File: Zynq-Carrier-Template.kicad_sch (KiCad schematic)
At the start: 5 parts, among them J1 Zynq_SoM

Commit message: Testing collab functionality
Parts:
- added J3: USB_C_Receptacle_USB2.0_16P, Connector_USB:USB_C_Receptacle_G-Switch_GT-USB-7010ASV, symbol Connector:USB_C_Receptacle_USB2.0_16P
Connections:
- new net: J3.A1 (GND), J3.A12 (GND), J3.B1 (GND), J3.B12 (GND)
- new net: J3.A4 (VBUS), J3.A9 (VBUS), J3.B4 (VBUS), J3.B9 (VBUS)
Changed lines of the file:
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@@
+	)
+	(symbol
+		(lib_id "Connector:USB_C_Receptacle_USB2.0_16P")
+		(at 232.41 130.81 0)
+		(unit 1)
+		(exclude_from_sim no)
+		(in_bom yes)
+		(on_board yes)
+		(dnp no)
+		(fields_autoplaced yes)
+		(property "Reference" "J3"
+			(at 232.41 107.95 0)
+			(effects
+				(font
+					(size 1.27 1.27)
+				)
+			)
+		)
+		(property "Value" "USB_C_Receptacle_USB2.0_16P"
+			(at 232.41 110.49 0)
+			(effects
+				(font
+					(size 1.27 1.27)
+				)
+			)
+		)
+		(property "Footprint" "Connector_USB:USB_C_Receptacle_G-Switch_GT-USB-7010ASV"
+			(at 236.22 130.81 0)
+			(effects
+				(font
+					(size 1.27 1.27)
+				)
+				(hide yes)
+			)
+		)
+		(property "Datasheet" "https://www.usb.org/sites/default/files/documents/usb_type-c.zip"
+			(at 236.22 130.81 0)
+			(effects
+				(font
+					(size 1.27 1.27)
+				)
+				(hide yes)
+			)
+		)
+		(property "Description" "USB 2.0-only 16P Type-C Receptacle connector"
+			(at 232.41 130.81 0)
+			(effects
+				(font
+					(size 1.27 1.27)
+				)
+				(hide yes)
+			)
+		)
+		(pin "A9"
+		)
+		(pin "A6"
+		)
+		(pin "A12"
+		)
+		(pin "B7"
+		)
+		(pin "B9"
+		)
+		(pin "B8"
+		)
+		(pin "B6"
+		)
+		(pin "A5"
+		)
+		(pin "B5"
+		)
+		(pin "B1"
+		)
+		(pin "A7"
+		)
+		(pin "A1"
+		)
+		(pin "A8"
+		)
+		(pin "A4"
+		)
+		(pin "B12"
+		)
+		(pin "S1"
+		)
+		(pin "B4"
+		)
+		(instances
+			(project ""
+				(path "/e0c786d3-4c71-488f-94d1-904eb052c2b4"
+					(reference "J3")
+					(unit 1)
+				)
+			)
+		)
 	)
 	(symbol

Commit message: Import BQ25629RYKR
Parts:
- added U1: BQ25629RYKR, BQ25629RYKR:RYK0018A-MFG, symbol BQ25629RYKR:BQ25629RYKR
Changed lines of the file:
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@@
+	)
+	(symbol
+		(lib_id "BQ25629RYKR:BQ25629RYKR")
+		(at 217.17 49.53 0)
+		(unit 1)
+		(exclude_from_sim no)
+		(in_bom yes)
+		(on_board yes)
+		(dnp no)
+		(fields_autoplaced yes)
+		(property "Reference" "U1"
+			(at 236.22 39.37 0)
+			(effects
+				(font
+					(size 1.524 1.524)
+				)
+			)
+		)
+		(property "Value" "BQ25629RYKR"
+			(at 236.22 41.91 0)
+			(effects
+				(font
+					(size 1.524 1.524)
+				)
+			)
+		)
+		(property "Footprint" "BQ25629RYKR:RYK0018A-MFG"
+			(at 217.17 49.53 0)
+			(effects
+				(font
+					(size 1.27 1.27)
+					(italic yes)
+				)
+				(hide yes)
+			)
+		)
+		(property "Datasheet" "https://www.ti.com/lit/gpn/bq25629"
+			(at 217.17 49.53 0)
+			(effects
+				(font
+					(size 1.27 1.27)
+					(italic yes)
+				)
+				(hide yes)
+			)
+		)
+		(property "Description" ""
+			(at 217.17 49.53 0)
+			(effects
+				(font
+					(size 1.27 1.27)
+				)
+				(hide yes)
+			)
+		)
+		(pin "17"
+		)
+		(pin "10"
+		)
+		(pin "18"
+		)
+		(pin "14"
+		)
+		(pin "3"
+		)
+		(pin "15"
+		)
+		(pin "7"
+		)
+		(pin "5"
+		)
+		(pin "8"
+		)
+		(pin "16"
+		)
+		(pin "1"
+		)
+		(pin "6"
+		)
+		(pin "9"
+		)
+		(pin "2"
+		)
+		(pin "4"
+		)
+		(pin "13"
+		)
+		(pin "11"
+		)
+		(pin "12"
+		)
+		(instances
+			(project ""
+				(path "/e0c786d3-4c71-488f-94d1-904eb052c2b4"
+					(reference "U1")
+					(unit 1)
+				)
+			)
+		)
 	)
 	(symbol

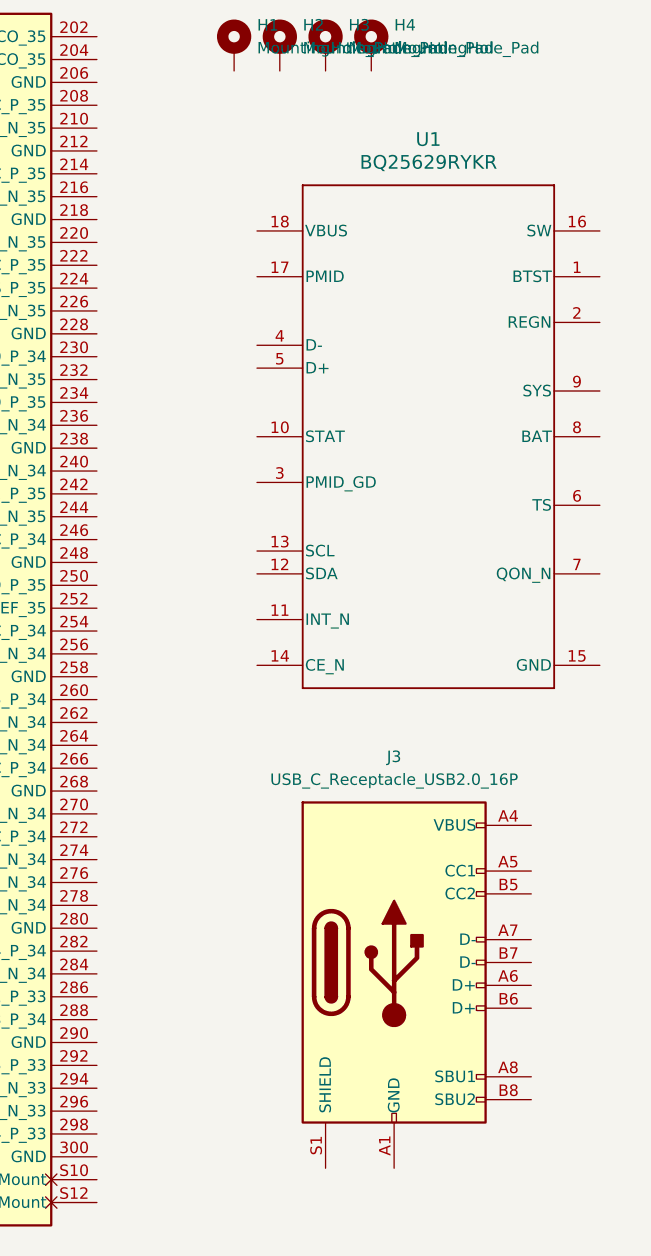
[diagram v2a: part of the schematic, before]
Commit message: Copper Fill demo
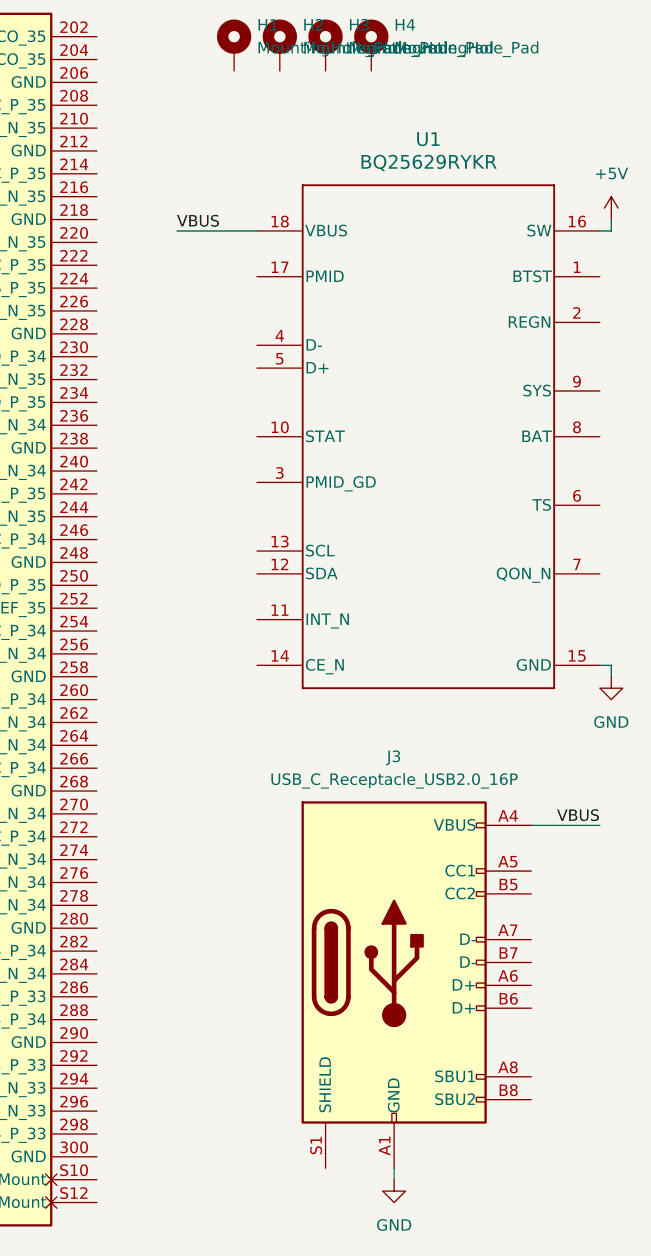
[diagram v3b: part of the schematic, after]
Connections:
- net GND: now reaches J3.A1 (GND), J3.A12 (GND), J3.B1 (GND), J3.B12 (GND)
- net GND: now also U1.15 (GND)
- net VBUS: now reaches J3.A4 (VBUS), J3.A9 (VBUS), J3.B4 (VBUS), J3.B9 (VBUS)
- net VBUS: now also U1.18 (VBUS)
- net +5V: now reaches U1.16 (SW)

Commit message: Import 1uH Inductor
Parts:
- added L1: P3519R-102J, 1uH_Inductor:IND_P3519R_API, symbol 1uH_Inductor:P3519R-102J
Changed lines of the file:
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@@
 (kicad_sch
-	(version 20231120)
+	(version 20250114)
 	(generator "eeschema")
-	(generator_version "8.0")
+	(generator_version "9.0")
 	(paper "A4")
 	(wire
@@
 	(label "VBUS"
 		(at 208.28 49.53 0)
-		(fields_autoplaced yes)
 		(effects
 			(font
@@
 	(label "VBUS"
 		(at 255.27 115.57 180)
-		(fields_autoplaced yes)
 		(effects
 			(font
@@
 	)
 	(symbol
+		(lib_id "1uH_Inductor:P3519R-102J")
+		(at 261.62 33.02 0)
+		(unit 1)
+		(exclude_from_sim no)
+		(in_bom yes)
+		(on_board yes)
+		(dnp no)
+		(fields_autoplaced yes)
+		(property "Reference" "L1"
+			(at 269.24 25.4 0)
+			(effects
+				(font
+					(size 1.524 1.524)
+				)
+			)
+		)
+		(property "Value" "P3519R-102J"
+			(at 269.24 27.94 0)
+			(effects
+				(font
+					(size 1.524 1.524)
+				)
+			)
+		)
+		(property "Footprint" "1uH_Inductor:IND_P3519R_API"
+			(at 261.62 33.02 0)
+			(effects
+				(font
+					(size 1.27 1.27)
+					(italic yes)
+				)
+				(hide yes)
+			)
+		)
+		(property "Datasheet" "P3519R-102J"
+			(at 261.62 33.02 0)
+			(effects
+				(font
+					(size 1.27 1.27)
+					(italic yes)
+				)
+				(hide yes)
+			)
+		)
+		(property "Description" ""
+			(at 261.62 33.02 0)
+			(effects
+				(font
+					(size 1.27 1.27)
+				)
+				(hide yes)
+			)
+		)
+		(pin "1"
+		)
+		(pin "2"
+		)
+		(instances
+			(project ""
+				(path "/e0c786d3-4c71-488f-94d1-904eb052c2b4"
+					(reference "L1")
+					(unit 1)
+				)
+			)
+		)
+	)
+	(symbol
 		(lib_id "Mechanical:MountingHole_Pad")
 		(at 219.71 29.21 0)
@@
 		)
 	)
+	(embedded_fonts no)
 )

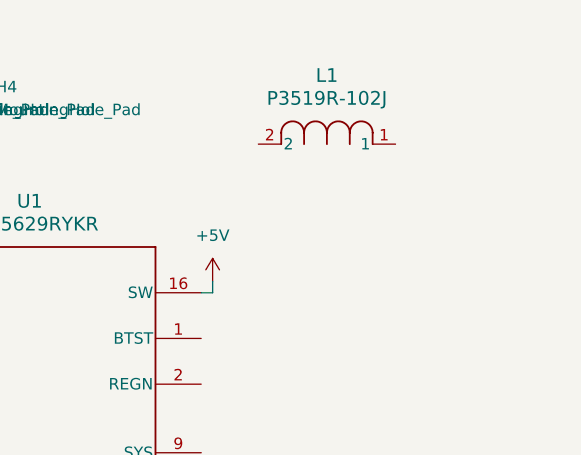
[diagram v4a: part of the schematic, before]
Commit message: Import JST_Pins and Inductor
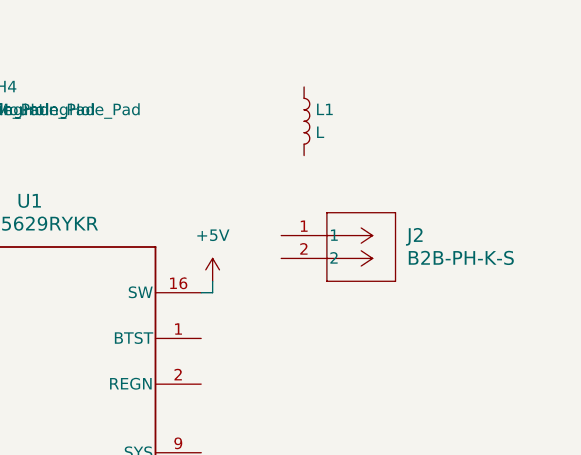
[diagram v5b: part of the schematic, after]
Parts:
- removed L1: P3519R-102J, 1uH_Inductor:IND_P3519R_API, symbol 1uH_Inductor:P3519R-102J
- added J2: B2B-PH-K-S, CONN2_B2B-PH-K-S_JST, symbol JST_Pins:B2B-PH-K-S
- added L1: L, Inductor_SMD:L_1008_2520Metric_Pad1.43x2.20mm_HandSolder, symbol Device:L
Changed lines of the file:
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@@
+	)
+	(symbol
+		(lib_id "JST_Pins:B2B-PH-K-S")
+		(at 264.16 43.18 0)
+		(unit 1)
+		(exclude_from_sim no)
+		(in_bom yes)
+		(on_board yes)
+		(dnp no)
+		(fields_autoplaced yes)
+		(property "Reference" "J2"
+			(at 278.13 43.1799 0)
+			(effects
+				(font
+					(size 1.524 1.524)
+				)
+				(justify left)
+			)
+		)
+		(property "Value" "B2B-PH-K-S"
+			(at 278.13 45.7199 0)
+			(effects
+				(font
+					(size 1.524 1.524)
+				)
+				(justify left)
+			)
+		)
+		(property "Footprint" "CONN2_B2B-PH-K-S_JST"
+			(at 264.16 43.18 0)
+			(effects
+				(font
+					(size 1.27 1.27)
+					(italic yes)
+				)
+				(hide yes)
+			)
+		)
+		(property "Datasheet" "B2B-PH-K-S"
+			(at 264.16 43.18 0)
+			(effects
+				(font
+					(size 1.27 1.27)
+					(italic yes)
+				)
+				(hide yes)
+			)
+		)
+		(property "Description" ""
+			(at 264.16 43.18 0)
+			(effects
+				(font
+					(size 1.27 1.27)
+				)
+				(hide yes)
+			)
+		)
+		(pin "2"
+		)
+		(pin "1"
+		)
+		(instances
+			(project ""
+				(path "/e0c786d3-4c71-488f-94d1-904eb052c2b4"
+					(reference "J2")
+					(unit 1)
+				)
+			)
+		)
 	)
 	(symbol
@@
 	)
 	(symbol
+		(lib_id "Device:L")
+		(at 266.7 30.48 0)
+		(unit 1)
+		(exclude_from_sim no)
+		(in_bom yes)
+		(on_board yes)
+		(dnp no)
+		(fields_autoplaced yes)
+		(property "Reference" "L1"
+			(at 267.97 29.2099 0)
+			(effects
+				(font
+					(size 1.27 1.27)
+				)
+				(justify left)
+			)
+		)
+		(property "Value" "L"
+			(at 267.97 31.7499 0)
+			(effects
+				(font
+					(size 1.27 1.27)
+				)
+				(justify left)
+			)
+		)
+		(property "Footprint" "Inductor_SMD:L_1008_2520Metric_Pad1.43x2.20mm_HandSolder"
+			(at 266.7 30.48 0)
+			(effects
+				(font
+					(size 1.27 1.27)
+				)
+				(hide yes)
+			)
+		)
+		(property "Datasheet" "~"
+			(at 266.7 30.48 0)
+			(effects
+				(font
+					(size 1.27 1.27)
+				)
+				(hide yes)
+			)
+		)
+		(property "Description" "Inductor"
+			(at 266.7 30.48 0)
+			(effects
+				(font
+					(size 1.27 1.27)
+				)
+				(hide yes)
+			)
+		)
+		(pin "2"
+		)
+		(pin "1"
+		)
+		(instances
+			(project ""
+				(path "/e0c786d3-4c71-488f-94d1-904eb052c2b4"
+					(reference "L1")
+					(unit 1)
+				)
+			)
+		)
+	)
+	(symbol
 		(lib_id "symbol_Zynq_SoM:Zynq_SoM")
 		(at 22.86 27.94 0)
@@
 					(unit 1)
 				)
-			)
-		)
-	)
-	(symbol
-		(lib_id "1uH_Inductor:P3519R-102J")
-		(at 261.62 33.02 0)
-		(unit 1)
-		(exclude_from_sim no)
-		(in_bom yes)
-		(on_board yes)
-		(dnp no)
-		(fields_autoplaced yes)
-		(property "Reference" "L1"
-			(at 269.24 25.4 0)
-			(effects
-				(font
-					(size 1.524 1.524)
-				)
-			)
-		)
-		(property "Value" "P3519R-102J"
-			(at 269.24 27.94 0)
-			(effects
-				(font
-					(size 1.524 1.524)
-				)
-			)
-		)
-		(property "Footprint" "1uH_Inductor:IND_P3519R_API"
-			(at 261.62 33.02 0)
-			(effects
-				(font
-					(size 1.27 1.27)
-					(italic yes)
-				)
-				(hide yes)
-			)
-		)
-		(property "Datasheet" "P3519R-102J"
-			(at 261.62 33.02 0)
-			(effects
-				(font
-					(size 1.27 1.27)
-					(italic yes)
-				)
-				(hide yes)
-			)
-		)
-		(property "Description" ""
-			(at 261.62 33.02 0)
-			(effects
-				(font
-					(size 1.27 1.27)
-				)
-				(hide yes)
-			)
-		)
-		(pin "1"
-		)
-		(pin "2"
-		)
-		(instances
-			(project ""
-				(path "/e0c786d3-4c71-488f-94d1-904eb052c2b4"
-					(reference "L1")
-					(unit 1)
-				)

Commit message: USB-C Schematic
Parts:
- added J4, J5: Conn_01x03, Connector_PinHeader_2.54mm:PinHeader_1x03_P2.54mm_Vertical, symbol Connector_Generic:Conn_01x03
- added R1, R2, R3: 5.1k, Resistor_SMD:R_0603_1608Metric, symbol Device:R_US
- added R4: 1M, Resistor_SMD:R_0603_1608Metric, symbol Device:R_US
- added R5: 100k, Resistor_SMD:R_0603_1608Metric, symbol Device:R_US
- added U12: SRV05-4, Package_TO_SOT_SMD:SOT-23-6, symbol Power_Protection:SRV05-4
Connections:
- net +5V: now also J1.1 (VIN), J1.10 (VIN), J1.11 (VIN), J1.12 (VIN), J1.13 (VIN), J1.14 (VIN), J1.2 (VIN), J1.3 (VIN), J1.4 (VIN), J1.5 (VIN), J1.6 (VIN), J1.7 (VIN), J1.8 (VIN), J1.9 (VIN)
- net GND: now also J1.104 (GND), J1.105 (GND), J1.106 (GND), J1.115 (GND), J1.116 (GND), J1.125 (GND), J1.126 (GND), J1.135 (GND), J1.136 (GND), J1.145 (GND), J1.146 (GND), J1.15 (GND), J1.155 (GND), J1.16 (GND), J1.165 (GND), J1.166 (GND), J1.17 (GND), J1.175 (GND), J1.176 (GND), J1.18 (GND), J1.185 (GND), J1.186 (GND), J1.195 (GND), J1.196 (GND), J1.197 (GND), J1.203 (GND), J1.206 (GND), J1.213 (GND), J1.218 (GND), J1.223 (GND), J1.228 (GND), J1.23 (GND), J1.233 (GND), J1.238 (GND), J1.243 (GND), J1.248 (GND), J1.253 (GND), J1.258 (GND), J1.263 (GND), J1.268 (GND), J1.273 (GND), J1.28 (GND), J1.280 (GND), J1.283 (GND), J1.290 (GND), J1.295 (GND), J1.300 (GND), J1.39 (GND), J1.44 (GND), J1.51 (GND), J1.62 (GND), J1.63 (GND), J1.72 (GND), J1.75 (GND), J1.81 (GND), J1.82 (GND), J1.87 (GND), J1.96 (GND), J1.99 (GND), J2.1, R1.1, R2.1, R4.2, R5.2, U12.2 (VN)
- net at J3.A5 (CC1): now also R1.2
- net USB_D+: now reaches J3.A6 (D+)
- net USB_D+: now also J3.B6 (D+), U12.3 (IO2)
- net USB_D-: now reaches J3.A7 (D-)
- net USB_D-: now also J3.B7 (D-), U12.1 (IO1)
- net at J3.B5 (CC2): now also R2.2
- net at J3.S1 (SHIELD): now also R4.1
- net VBAT: now reaches J2.2
- net USB_POW_D-: now reaches U1.4 (D-)
- net USB_POW_D-: now also J4.1 (Pin_1)
- net USB_POW_D+: now reaches U1.5 (D+)
- net USB_POW_D+: now also J5.1 (Pin_1)
- net USB_SOM_D-: now reaches J1.30 (USB_D-)
- net USB_SOM_D-: now also J4.2 (Pin_2), J4.3 (Pin_3)
- net USB_SOM_D+: now reaches J1.32 (USB_D+)
- net USB_SOM_D+: now also J5.2 (Pin_2), J5.3 (Pin_3)
- net VBUS renamed V_USB
- net V_USB: now also R3.1, R5.1
- new net: R3.2, U12.5 (VP)
- no-connect marks 0 -> 4
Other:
- moved on the sheet: H1, H2, H3, H4, J1A, J1B, J1C, J2, J3, L1, U1
